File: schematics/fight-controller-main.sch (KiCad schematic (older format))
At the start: 0 parts

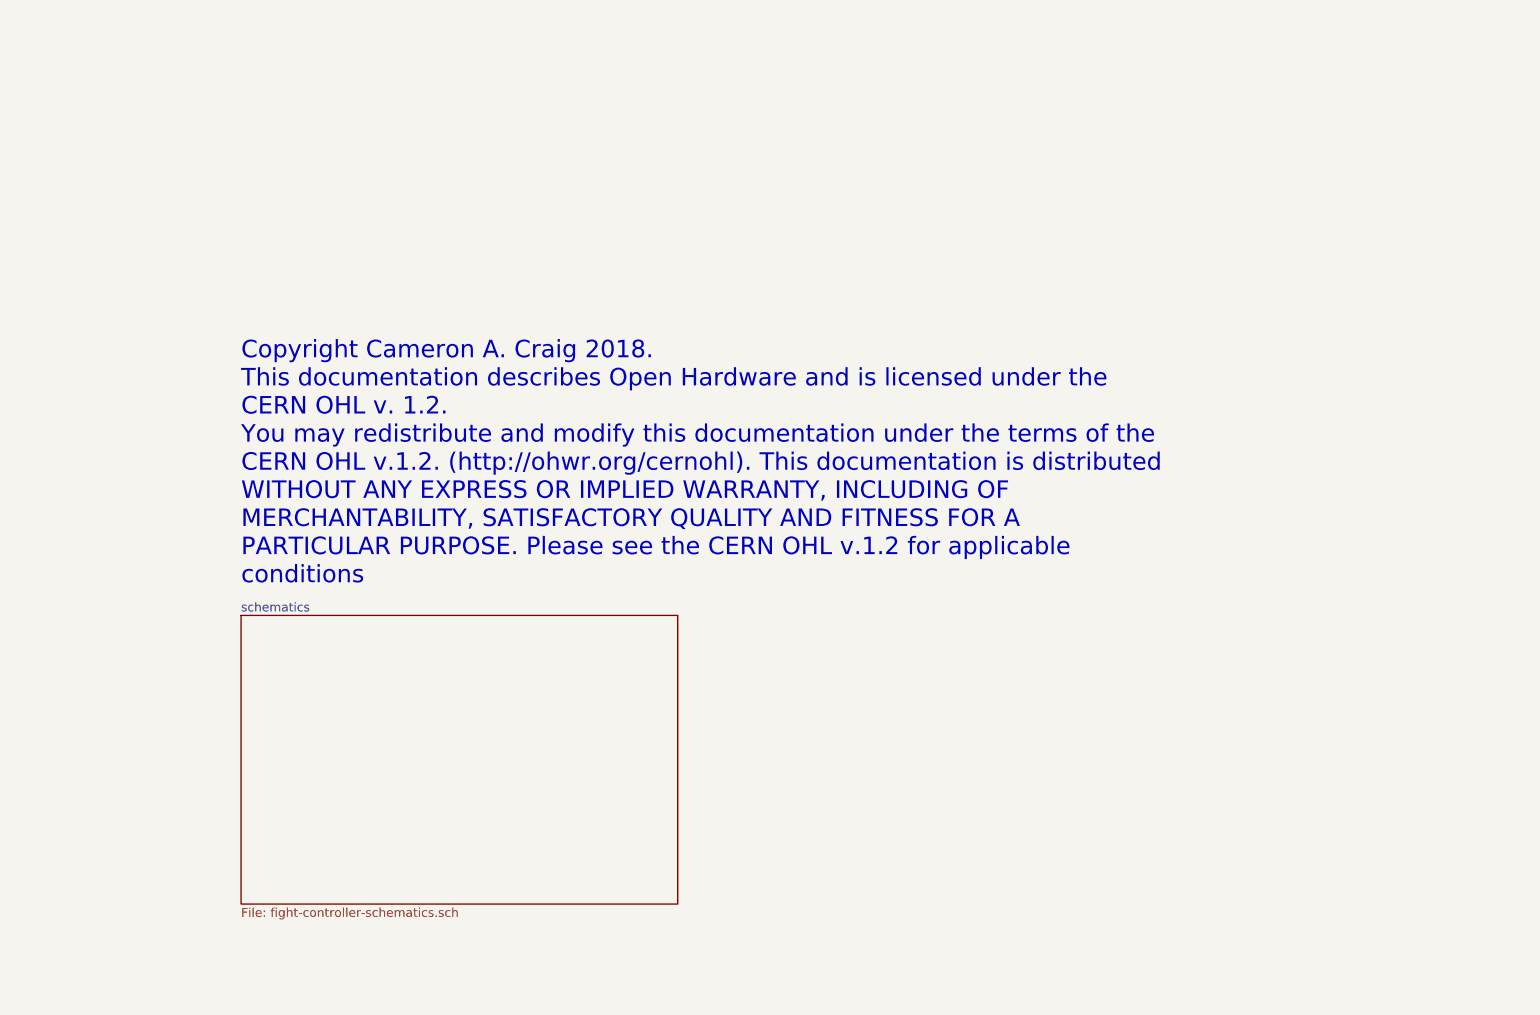
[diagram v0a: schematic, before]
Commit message: Started v2.x work, integrating developement boards into PCB.
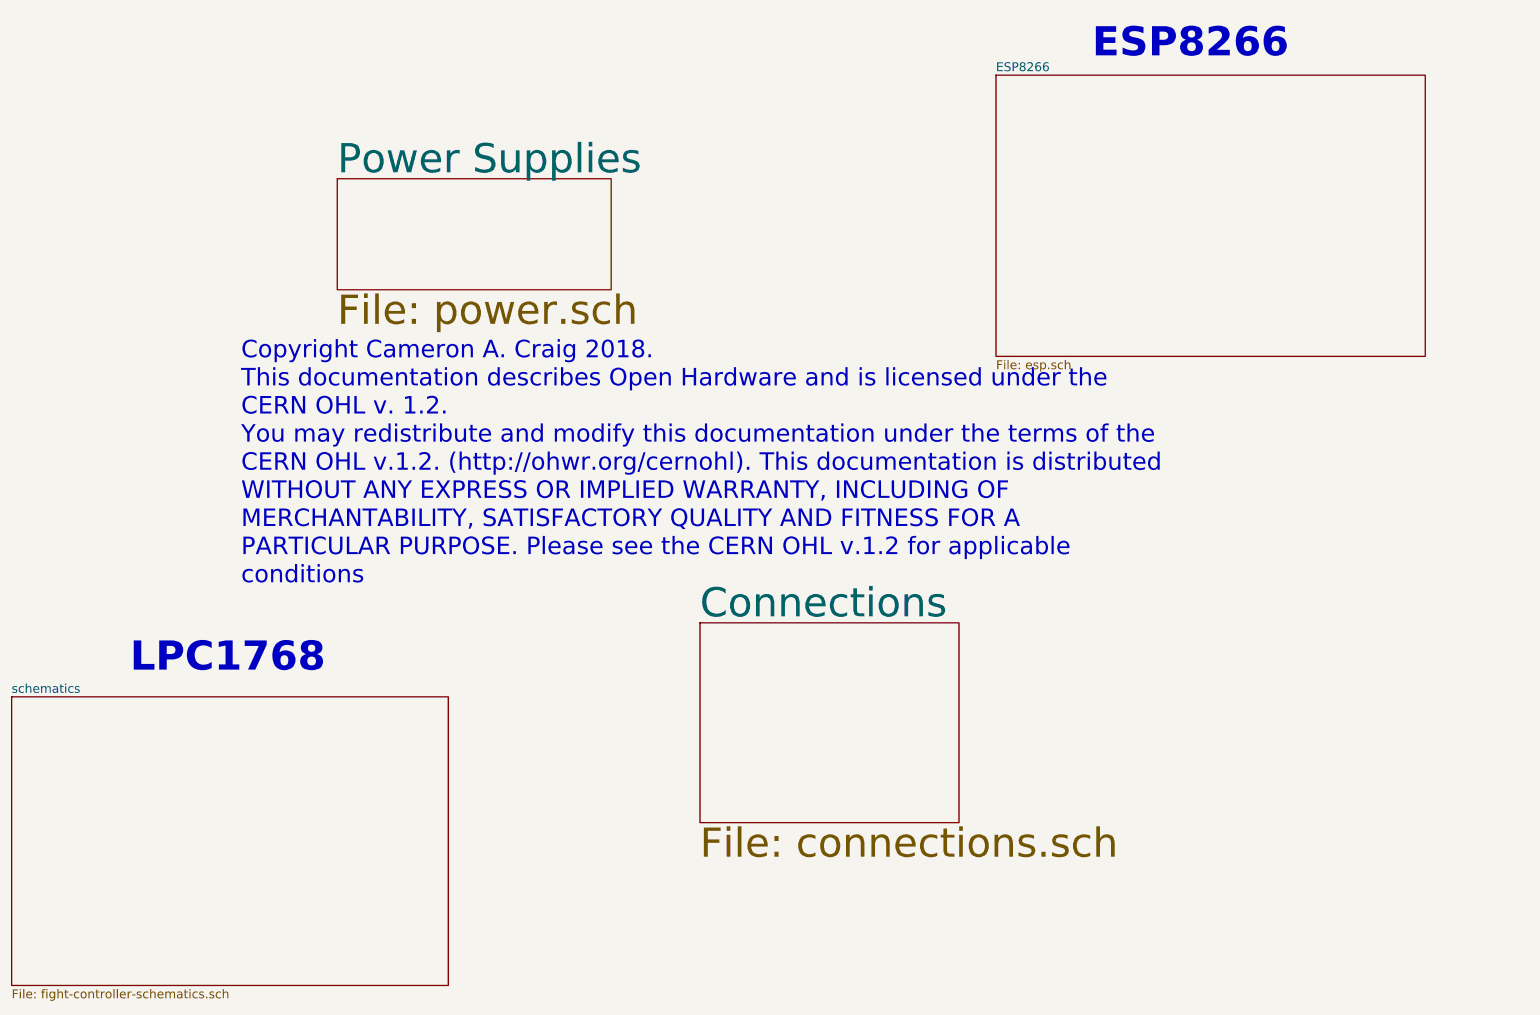
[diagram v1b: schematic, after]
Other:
- note added: "ESP8266"
- note added: "LPC1768"
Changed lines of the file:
@@
 EESchema Schematic File Version 2
-LIBS:power
-LIBS:device
-LIBS:switches
-LIBS:relays
-LIBS:motors
-LIBS:transistors
-LIBS:conn
-LIBS:linear
-LIBS:regul
-LIBS:74xx
-LIBS:cmos4000
-LIBS:adc-dac
-LIBS:memory
-LIBS:xilinx
-LIBS:microcontrollers
-LIBS:dsp
-LIBS:microchip
-LIBS:analog_switches
-LIBS:motorola
-LIBS:texas
-LIBS:intel
-LIBS:audio
-LIBS:interface
-LIBS:digital-audio
-LIBS:philips
-LIBS:display
-LIBS:cypress
-LIBS:siliconi
-LIBS:opto
-LIBS:atmel
-LIBS:contrib
-LIBS:valves
 LIBS:triforce-fight-controller
 LIBS:fight-controller-main-cache
@@
 $Descr A4 11693 8268
 encoding utf-8
-Sheet 1 2
+Sheet 1 5
 Title "Triforce Fight Controller"
 Date "2018-01-22"
@@
 Copyright Cameron A. Craig 2018.\nThis documentation describes Open Hardware and is licensed under the\nCERN OHL v. 1.2.\nYou may redistribute and modify this documentation under the terms of the\nCERN OHL v.1.2. (http://ohwr.org/cernohl). This documentation is distributed\nWITHOUT ANY EXPRESS OR IMPLIED WARRANTY, INCLUDING OF\nMERCHANTABILITY, SATISFACTORY QUALITY AND FITNESS FOR A\nPARTICULAR PURPOSE. Please see the CERN OHL v.1.2 for applicable\nconditions
 $Sheet
-S 2500 4600 2950 1950
+S 950  5150 2950 1950
 U 5A664795
 F0 "schematics" 60
 F1 "fight-controller-schematics.sch" 60
 $EndSheet
+$Sheet
+S 7600 950  2900 1900
+U 5A916412
+F0 "ESP8266" 60
+F1 "esp.sch" 60
+$EndSheet
+Text Notes 8250 850  0    197  ~ 39
+ESP8266
+Text Notes 1750 5000 0    197  ~ 39
+LPC1768
+$Sheet
+S 5600 4650 1750 1350
+U 5A917F9B
+F0 "Connections" 197
+F1 "connections.sch" 197
+$EndSheet
+$Sheet
+S 3150 1650 1850 750
+U 5A918A1A
+F0 "Power Supplies" 197
+F1 "power.sch" 197
+$EndSheet
 $EndSCHEMATC
